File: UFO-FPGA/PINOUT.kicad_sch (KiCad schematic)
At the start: 4 parts, among them J2 Power, J3 Digital, J4 Digital/PWM, J5 Digital

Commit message: Opamp gemaakt van de ADC
Enkel nog begrijpen wat VDC is. Aan docent vragen?
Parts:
- removed J2: Power, Connector_PinSocket_2.54mm:PinSocket_1x08_P2.54mm_Vertical, symbol Connector_Generic:Conn_01x08
- removed J3: Digital, Connector_PinSocket_2.54mm:PinSocket_1x06_P2.54mm_Vertical, symbol Connector_Generic:Conn_01x06
- removed J4: Digital/PWM, Connector_PinSocket_2.54mm:PinSocket_1x10_P2.54mm_Vertical, symbol Connector_Generic:Conn_01x10
- removed J5: Digital, Connector_PinSocket_2.54mm:PinSocket_1x08_P2.54mm_Vertical, symbol Connector_Generic:Conn_01x08
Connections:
- no-connect marks 1 -> 0

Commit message: IO and power
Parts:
- added J2: Power, Connector_PinSocket_2.54mm:PinSocket_1x08_P2.54mm_Vertical, symbol Connector_Generic:Conn_01x08
- added J3: Digital, Connector_PinSocket_2.54mm:PinSocket_1x06_P2.54mm_Vertical, symbol Connector_Generic:Conn_01x06
- added J4: Digital/PWM, Connector_PinSocket_2.54mm:PinSocket_1x10_P2.54mm_Vertical, symbol Connector_Generic:Conn_01x10
- added J5: Digital, Connector_PinSocket_2.54mm:PinSocket_1x08_P2.54mm_Vertical, symbol Connector_Generic:Conn_01x08
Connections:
- new net +3V3: J2.4 (Pin_4)
- new net +5V: J2.5 (Pin_5)
- new net AIN1: J3.5 (Pin_5)
- new net AIN2: J3.6 (Pin_6)
- new net GND: J2.6 (Pin_6), J2.7 (Pin_7), J4.4 (Pin_4)
- new net PIN-1: J4.1 (Pin_1)
- new net PIN-10: J5.1 (Pin_1)
- new net PIN-11: J5.2 (Pin_2)
- new net PIN-12: J5.3 (Pin_3)
- new net PIN-13: J5.4 (Pin_4)
- new net PIN-14: J5.5 (Pin_5)
- new net PIN-15: J5.6 (Pin_6)
- new net PIN-16: J5.7 (Pin_7)
- new net PIN-17: J5.8 (Pin_8)
- new net PIN-18: J3.1 (Pin_1)
- new net PIN-19: J3.2 (Pin_2)
- new net PIN-2: J4.2 (Pin_2)
- new net PIN-20: J3.3 (Pin_3)
- new net PIN-21: J3.4 (Pin_4)
- new net PIN-22: J2.2 (Pin_2)
- new net PIN-23: J2.3 (Pin_3)
- new net PIN-3: J4.3 (Pin_3)
- new net PIN-4: J4.5 (Pin_5)
- new net PIN-5: J4.6 (Pin_6)
- new net PIN-6: J4.7 (Pin_7)
- new net PIN-7: J4.8 (Pin_8)
- new net PIN-8: J4.9 (Pin_9)
- new net PIN-9: J4.10 (Pin_10)
- new net Vin: J2.8 (Pin_8)
- no-connect marks 0 -> 1

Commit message: Revision
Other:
- company: (none) -> Universal-Field-Objects
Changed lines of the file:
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@@
   (paper "A4")
   (title_block
-    (date "2023-04-22")
-    (rev "V0.1")
+    (date "2023-04-25")
+    (rev "V0.5")
+    (company "Universal-Field-Objects")
   )
   (junction (at 121.92 80.01) (diameter 1.016) (color 0 0 0 0)

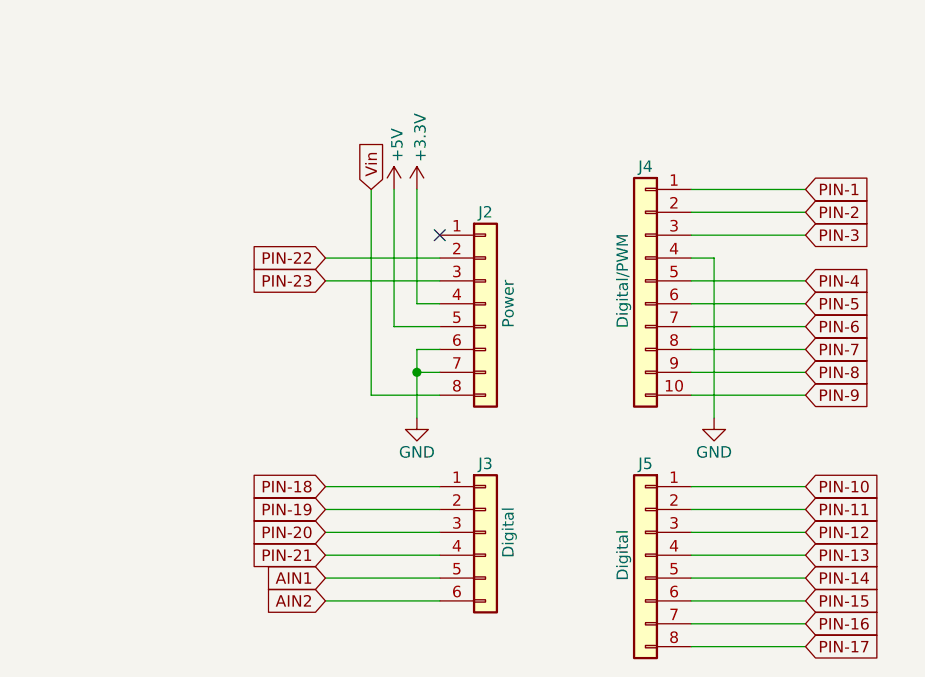
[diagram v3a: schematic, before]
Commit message: PCB and footprint
Added foorprints and moved on pcb layout
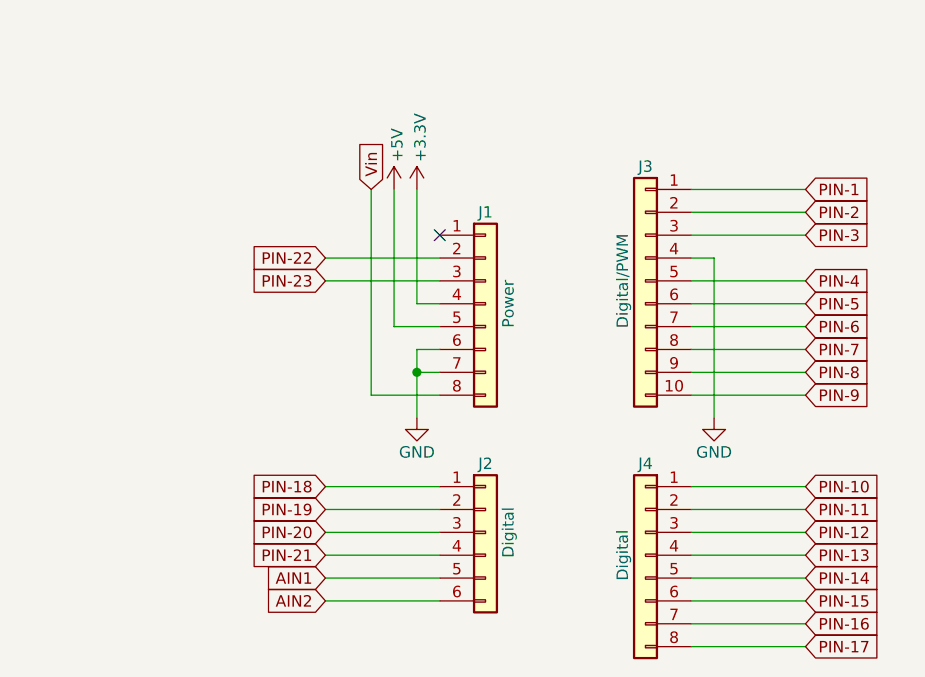
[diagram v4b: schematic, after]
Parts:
- renumbered J2 to J1, J3 to J2, J4 to J3, J5 to J4
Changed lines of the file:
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@@
   (symbol (lib_id "Connector_Generic:Conn_01x08") (at 129.54 72.39 0) (unit 1)
     (in_bom yes) (on_board yes) (dnp no)
-    (property "Reference" "J2" (at 129.54 62.23 0)
+    (property "Reference" "J1" (at 129.54 62.23 0)
       (effects (font (size 1.27 1.27)))
     )
@@
       (project "UFO-FPGA"
         (path "/b3168f6a-c732-41d3-aeeb-d97dd2f1bb65/8a110dcf-7b5f-4510-96dd-3ef5ec8aca05"
-          (reference "J2") (unit 1)
+          (reference "J1") (unit 1)
         )
       )
@@
   (symbol (lib_id "Connector_Generic:Conn_01x08") (at 147.32 100.33 0) (mirror y) (unit 1)
     (in_bom yes) (on_board yes) (dnp no)
-    (property "Reference" "J5" (at 147.32 90.17 0)
+    (property "Reference" "J4" (at 147.32 90.17 0)
       (effects (font (size 1.27 1.27)))
     )
@@
       (project "UFO-FPGA"
         (path "/b3168f6a-c732-41d3-aeeb-d97dd2f1bb65/8a110dcf-7b5f-4510-96dd-3ef5ec8aca05"
-          (reference "J5") (unit 1)
+          (reference "J4") (unit 1)
         )
       )
@@
   (symbol (lib_id "Connector_Generic:Conn_01x10") (at 147.32 69.85 0) (mirror y) (unit 1)
     (in_bom yes) (on_board yes) (dnp no)
-    (property "Reference" "J4" (at 147.32 57.15 0)
+    (property "Reference" "J3" (at 147.32 57.15 0)
       (effects (font (size 1.27 1.27)))
     )
@@
       (project "UFO-FPGA"
         (path "/b3168f6a-c732-41d3-aeeb-d97dd2f1bb65/8a110dcf-7b5f-4510-96dd-3ef5ec8aca05"
-          (reference "J4") (unit 1)
+          (reference "J3") (unit 1)
         )
       )
@@
   (symbol (lib_id "Connector_Generic:Conn_01x06") (at 129.54 97.79 0) (unit 1)
     (in_bom yes) (on_board yes) (dnp no)
-    (property "Reference" "J3" (at 129.54 90.17 0)
+    (property "Reference" "J2" (at 129.54 90.17 0)
       (effects (font (size 1.27 1.27)))
     )
@@
       (project "UFO-FPGA"
         (path "/b3168f6a-c732-41d3-aeeb-d97dd2f1bb65/8a110dcf-7b5f-4510-96dd-3ef5ec8aca05"
-          (reference "J3") (unit 1)
+          (reference "J2") (unit 1)
         )
       )

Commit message: PCB planes
Added:
added Power plane +1v2, +3v3 and +5v on layer 4
Ground plane on layer 2 and 5
Added signal layer 1,3 and 6
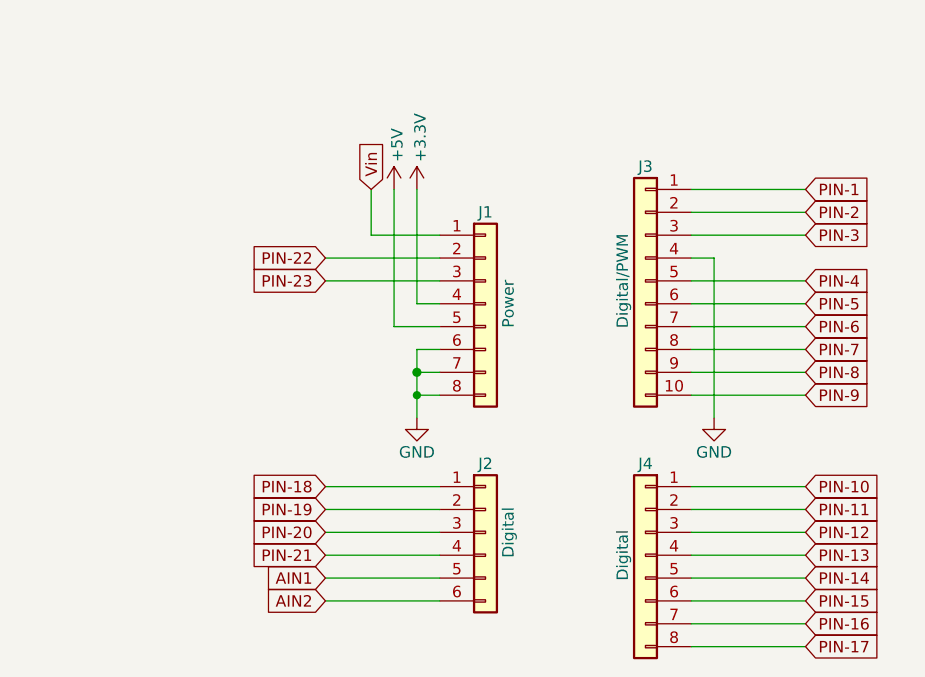
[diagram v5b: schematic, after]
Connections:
- net GND: now also J1.8 (Pin_8)
- net Vin: now also J1.1 (Pin_1); no longer J1.8 (Pin_8)
- no-connect marks 1 -> 0
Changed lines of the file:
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@@
   (junction (at 121.92 80.01) (diameter 1.016) (color 0 0 0 0)
   )
-  (no_connect (at 124.46 64.77))
+  (junction (at 121.92 82.55) (diameter 0) (color 0 0 0 0)
+  )
+  (wire (pts (xy 121.92 82.55) (xy 124.46 82.55))
+    (stroke (width 0) (type default))
+  )
   (wire (pts (xy 152.4 97.79) (xy 165.1 97.79))
     (stroke (width 0) (type solid))
+  )
+  (wire (pts (xy 116.84 64.77) (xy 124.46 64.77))
+    (stroke (width 0) (type default))
   )
   (wire (pts (xy 152.4 105.41) (xy 165.1 105.41))
@@
     (stroke (width 0) (type solid))
   )
+  (wire (pts (xy 116.84 64.77) (xy 116.84 59.69))
+    (stroke (width 0) (type solid))
+  )
   (wire (pts (xy 111.76 67.31) (xy 124.46 67.31))
     (stroke (width 0) (type default))
@@
     (stroke (width 0) (type solid))
   )
-  (wire (pts (xy 124.46 82.55) (xy 116.84 82.55))
-    (stroke (width 0) (type solid))
-  )
   (wire (pts (xy 152.4 80.01) (xy 165.1 80.01))
-    (stroke (width 0) (type solid))
-  )
-  (wire (pts (xy 116.84 82.55) (xy 116.84 59.69))
     (stroke (width 0) (type solid))
   )
@@
     (stroke (width 0) (type default))
   )
-  (wire (pts (xy 121.92 80.01) (xy 121.92 85.09))
+  (wire (pts (xy 121.92 80.01) (xy 121.92 82.55))
     (stroke (width 0) (type solid))
   )
@@
     (stroke (width 0) (type solid))
   )
+  (wire (pts (xy 121.92 82.55) (xy 121.92 85.09))
+    (stroke (width 0) (type solid))
+  )

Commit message: PCB
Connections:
- net AIN1 is gone; now on net GND: J2.5 (Pin_5)
- net AIN2 renamed AIN1_O
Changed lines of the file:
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@@
-    (stroke (width 0) (type solid))
-  )
-  (wire (pts (xy 111.76 105.41) (xy 124.46 105.41))
     (stroke (width 0) (type solid))
   )
@@
     (stroke (width 0) (type solid))
   )
+  (wire (pts (xy 111.76 105.41) (xy 124.46 105.41))
+    (stroke (width 0) (type default))
+  )
   (wire (pts (xy 152.4 107.95) (xy 165.1 107.95))
     (stroke (width 0) (type solid))
@@
     )
   )
-  (global_label "AIN1" (shape input) (at 111.76 102.87 180) (fields_autoplaced)
-    (effects (font (size 1.27 1.27)) (justify right))
-    (property "Intersheetrefs" "${INTERSHEET_REFS}" (at 104.6208 102.87 0)
-      (effects (font (size 1.27 1.27)) (justify right) hide)
-    )
-  )
   (global_label "PIN-17" (shape input) (at 165.1 110.49 0) (fields_autoplaced)
     (effects (font (size 1.27 1.27)) (justify left))
@@
     )
   )
-  (global_label "AIN2" (shape input) (at 111.76 105.41 180) (fields_autoplaced)
-    (effects (font (size 1.27 1.27)) (justify right))
-    (property "Intersheetrefs" "${INTERSHEET_REFS}" (at 104.6208 105.41 0)
+  (global_label "AIN1_O" (shape input) (at 111.76 105.41 180) (fields_autoplaced)
+    (effects (font (size 1.27 1.27)) (justify right))
+    (property "Intersheetrefs" "${INTERSHEET_REFS}" (at 102.3227 105.41 0)
       (effects (font (size 1.27 1.27)) (justify right) hide)
     )
@@
     (property "Intersheetrefs" "${INTERSHEET_REFS}" (at 175.2025 102.87 0)
       (effects (font (size 1.27 1.27)) (justify left) hide)
+    )
+  )
+  (symbol (lib_id "power:GND") (at 121.92 85.09 0) (unit 1)
+    (in_bom yes) (on_board yes) (dnp no) (fields_autoplaced)
+    (property "Reference" "#PWR050" (at 121.92 91.44 0)
+      (effects (font (size 1.27 1.27)) hide)
+    )
+    (property "Value" "GND" (at 121.92 89.2255 0)
+      (effects (font (size 1.27 1.27)))
+    )
+    (property "Footprint" "" (at 121.92 85.09 0)
+      (effects (font (size 1.27 1.27)) hide)
+    )
+    (property "Datasheet" "" (at 121.92 85.09 0)
+      (effects (font (size 1.27 1.27)) hide)
+    )
+    (pin "1")
+    (instances
+      (project "UFO-FPGA"
+        (path "/b3168f6a-c732-41d3-aeeb-d97dd2f1bb65/8a110dcf-7b5f-4510-96dd-3ef5ec8aca05"
+          (reference "#PWR050") (unit 1)
+        )
+      )
     )
   )
   (symbol (lib_id "power:+5V") (at 119.38 59.69 0) (unit 1)
     (in_bom yes) (on_board yes) (dnp no)
-    (property "Reference" "#PWR080" (at 119.38 63.5 0)
-      (effects (font (size 1.27 1.27)) hide)
-    )
-    (property "Value" "+5V" (at 119.7356 56.642 90)
-      (effects (font (size 1.27 1.27)) (justify left))
+    (property "Reference" "#PWR052" (at 119.38 63.5 0)
+      (effects (font (size 1.27 1.27)) hide)
+    )
+    (property "Value" "+5V" (at 119.38 54.61 90)
+      (effects (font (size 1.27 1.27)))
     )
     (property "Footprint" "" (at 119.38 59.69 0)
-      (effects (font (size 1.27 1.27)))
+      (effects (font (size 1.27 1.27)) hide)
     )
     (property "Datasheet" "" (at 119.38 59.69 0)
-      (effects (font (size 1.27 1.27)))
-    )
-    (pin "1")
-    (instances
-      (project "UFO-FPGA"
-        (path "/b3168f6a-c732-41d3-aeeb-d97dd2f1bb65/8a110dcf-7b5f-4510-96dd-3ef5ec8aca05"
-          (reference "#PWR080") (unit 1)
-        )
-      )
-      (project "PINOUT"
-        (path "/de984c47-a4b3-4404-8f6d-5958f9d846d6"
-          (reference "#PWR059") (unit 1)
-        )
-      )
-      (project "Uno-Template"
-        (path "/e63e39d7-6ac0-4ffd-8aa3-1841a4541b55"
-          (reference "#PWR02") (unit 1)
-        )
-      )
-    )
-  )
-  (symbol (lib_id "power:GND") (at 154.94 85.09 0) (unit 1)
-    (in_bom yes) (on_board yes) (dnp no)
-    (property "Reference" "#PWR083" (at 154.94 91.44 0)
-      (effects (font (size 1.27 1.27)) hide)
-    )
-    (property "Value" "GND" (at 154.94 88.9 0)
-      (effects (font (size 1.27 1.27)))
-    )
-    (property "Footprint" "" (at 154.94 85.09 0)
-      (effects (font (size 1.27 1.27)))
-    )
-    (property "Datasheet" "" (at 154.94 85.09 0)
-      (effects (font (size 1.27 1.27)))
-    )
-    (pin "1")
-    (instances
-      (project "UFO-FPGA"
-        (path "/b3168f6a-c732-41d3-aeeb-d97dd2f1bb65/8a110dcf-7b5f-4510-96dd-3ef5ec8aca05"
-          (reference "#PWR083") (unit 1)
-        )
-      )
-      (project "PINOUT"
-        (path "/de984c47-a4b3-4404-8f6d-5958f9d846d6"
-          (reference "#PWR062") (unit 1)
-        )
-      )
-      (project "Uno-Template"
-        (path "/e63e39d7-6ac0-4ffd-8aa3-1841a4541b55"
-          (reference "#PWR05") (unit 1)
+      (effects (font (size 1.27 1.27)) hide)
+    )
+    (pin "1")
+    (instances
+      (project "UFO-FPGA"
+        (path "/b3168f6a-c732-41d3-aeeb-d97dd2f1bb65/8a110dcf-7b5f-4510-96dd-3ef5ec8aca05"
+          (reference "#PWR052") (unit 1)
         )
       )
@@
   (symbol (lib_id "power:+3V3") (at 121.92 59.69 0) (unit 1)
     (in_bom yes) (on_board yes) (dnp no)
-    (property "Reference" "#PWR081" (at 121.92 63.5 0)
-      (effects (font (size 1.27 1.27)) hide)
-    )
-    (property "Value" "+3.3V" (at 122.301 56.642 90)
-      (effects (font (size 1.27 1.27)) (justify left))
+    (property "Reference" "#PWR053" (at 121.92 63.5 0)
+      (effects (font (size 1.27 1.27)) hide)
+    )
+    (property "Value" "+3V3" (at 121.92 53.975 90)
+      (effects (font (size 1.27 1.27)))
     )
     (property "Footprint" "" (at 121.92 59.69 0)
-      (effects (font (size 1.27 1.27)))
+      (effects (font (size 1.27 1.27)) hide)
     )
     (property "Datasheet" "" (at 121.92 59.69 0)
-      (effects (font (size 1.27 1.27)))
-    )
-    (pin "1")
-    (instances
-      (project "UFO-FPGA"
-        (path "/b3168f6a-c732-41d3-aeeb-d97dd2f1bb65/8a110dcf-7b5f-4510-96dd-3ef5ec8aca05"
-          (reference "#PWR081") (unit 1)
-        )
-      )
-      (project "PINOUT"
-        (path "/de984c47-a4b3-4404-8f6d-5958f9d846d6"
-          (reference "#PWR060") (unit 1)
-        )
-      )
-      (project "Uno-Template"
-        (path "/e63e39d7-6ac0-4ffd-8aa3-1841a4541b55"
-          (reference "#PWR03") (unit 1)
+      (effects (font (size 1.27 1.27)) hide)
+    )
+    (pin "1")
+    (instances
+      (project "UFO-FPGA"
+        (path "/b3168f6a-c732-41d3-aeeb-d97dd2f1bb65/8a110dcf-7b5f-4510-96dd-3ef5ec8aca05"
+          (reference "#PWR053") (unit 1)
+        )
+      )
+    )
+  )
+  (symbol (lib_id "power:GND") (at 154.94 85.09 0) (unit 1)
+    (in_bom yes) (on_board yes) (dnp no) (fields_autoplaced)
+    (property "Reference" "#PWR051" (at 154.94 91.44 0)
+      (effects (font (size 1.27 1.27)) hide)
+    )
+    (property "Value" "GND" (at 154.94 89.2255 0)
+      (effects (font (size 1.27 1.27)))
+    )
+    (property "Footprint" "" (at 154.94 85.09 0)
+      (effects (font (size 1.27 1.27)) hide)
+    )
+    (property "Datasheet" "" (at 154.94 85.09 0)
+      (effects (font (size 1.27 1.27)) hide)
+    )
+    (pin "1")
+    (instances
+      (project "UFO-FPGA"
+        (path "/b3168f6a-c732-41d3-aeeb-d97dd2f1bb65/8a110dcf-7b5f-4510-96dd-3ef5ec8aca05"
+          (reference "#PWR051") (unit 1)
+        )
+      )
+    )
+  )
+  (symbol (lib_id "power:GND") (at 111.76 102.87 270) (unit 1)
+    (in_bom yes) (on_board yes) (dnp no) (fields_autoplaced)
+    (property "Reference" "#PWR054" (at 105.41 102.87 0)
+      (effects (font (size 1.27 1.27)) hide)
+    )
+    (property "Value" "GND" (at 108.5851 103.1868 90)
+      (effects (font (size 1.27 1.27)) (justify right))
+    )
+    (property "Footprint" "" (at 111.76 102.87 0)
+      (effects (font (size 1.27 1.27)) hide)
+    )
+    (property "Datasheet" "" (at 111.76 102.87 0)
+      (effects (font (size 1.27 1.27)) hide)
+    )
+    (pin "1")
+    (instances
+      (project "UFO-FPGA"
+        (path "/b3168f6a-c732-41d3-aeeb-d97dd2f1bb65/8a110dcf-7b5f-4510-96dd-3ef5ec8aca05"
+          (reference "#PWR054") (unit 1)
         )
       )
@@
         )
       )
-    )
-  )
-  (symbol (lib_id "power:GND") (at 121.92 85.09 0) (unit 1)
-    (in_bom yes) (on_board yes) (dnp no)
-    (property "Reference" "#PWR082" (at 121.92 91.44 0)
-      (effects (font (size 1.27 1.27)) hide)
-    )
-    (property "Value" "GND" (at 121.92 88.9 0)
-      (effects (font (size 1.27 1.27)))
-    )
-    (property "Footprint" "" (at 121.92 85.09 0)
-      (effects (font (size 1.27 1.27)))
-    )
-    (property "Datasheet" "" (at 121.92 85.09 0)
-      (effects (font (size 1.27 1.27)))
-    )
-    (pin "1")
-    (instances
-      (project "UFO-FPGA"
-        (path "/b3168f6a-c732-41d3-aeeb-d97dd2f1bb65/8a110dcf-7b5f-4510-96dd-3ef5ec8aca05"
-          (reference "#PWR082") (unit 1)
-        )
-      )
-      (project "PINOUT"
-        (path "/de984c47-a4b3-4404-8f6d-5958f9d846d6"
-          (reference "#PWR061") (unit 1)
-        )
-      )
-      (project "Uno-Template"
-        (path "/e63e39d7-6ac0-4ffd-8aa3-1841a4541b55"
-          (reference "#PWR04") (unit 1)
-        )
-      )
